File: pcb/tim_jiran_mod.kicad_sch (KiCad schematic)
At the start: 110 parts, among them J3 MJ-4PP-9, J6 MJ-4PP-9, SW1 SW_PUSH, SW10 SW_PUSH, SW11 SW_PUSH, SW12 SW_PUSH, SW13 SW_PUSH, SW14 SW_PUSH, SW15 SW_PUSH, SW16 SW_PUSH, SW17 SW_PUSH, SW18 SW_PUSH, SW19 SW_RESET, SW2 SW_PUSH, SW20 SW_PUSH, SW21 SW_PUSH, SW22 SW_PUSH, SW23 SW_PUSH, SW24 SW_PUSH, SW25 SW_PUSH, SW26 SW_PUSH, SW27 SW_PUSH, SW28 SW_PUSH, SW29 SW_PUSH, SW3 SW_PUSH, SW30 SW_PUSH, SW31 SW_PUSH, SW32 SW_PUSH, SW33 SW_PUSH, SW34 SW_PUSH, SW35 SW_PUSH, SW36 SW_PUSH, SW37 SW_PUSH, SW38 SW_PUSH, SW39 SW_PUSH, SW4 SW_PUSH, SW40 SW_PUSH, SW41 SW_PUSH, SW42 SW_RESET, SW43 SW_PUSH, SW44 SW_PUSH, SW45 SW_PUSH, SW46 SW_PUSH, SW5 SW_PUSH, SW6 SW_PUSH, SW7 SW_PUSH, SW8 SW_PUSH, SW9 SW_PUSH, U1 Raspberry_Pie_Pico, U2 Raspberry_Pie_Pico

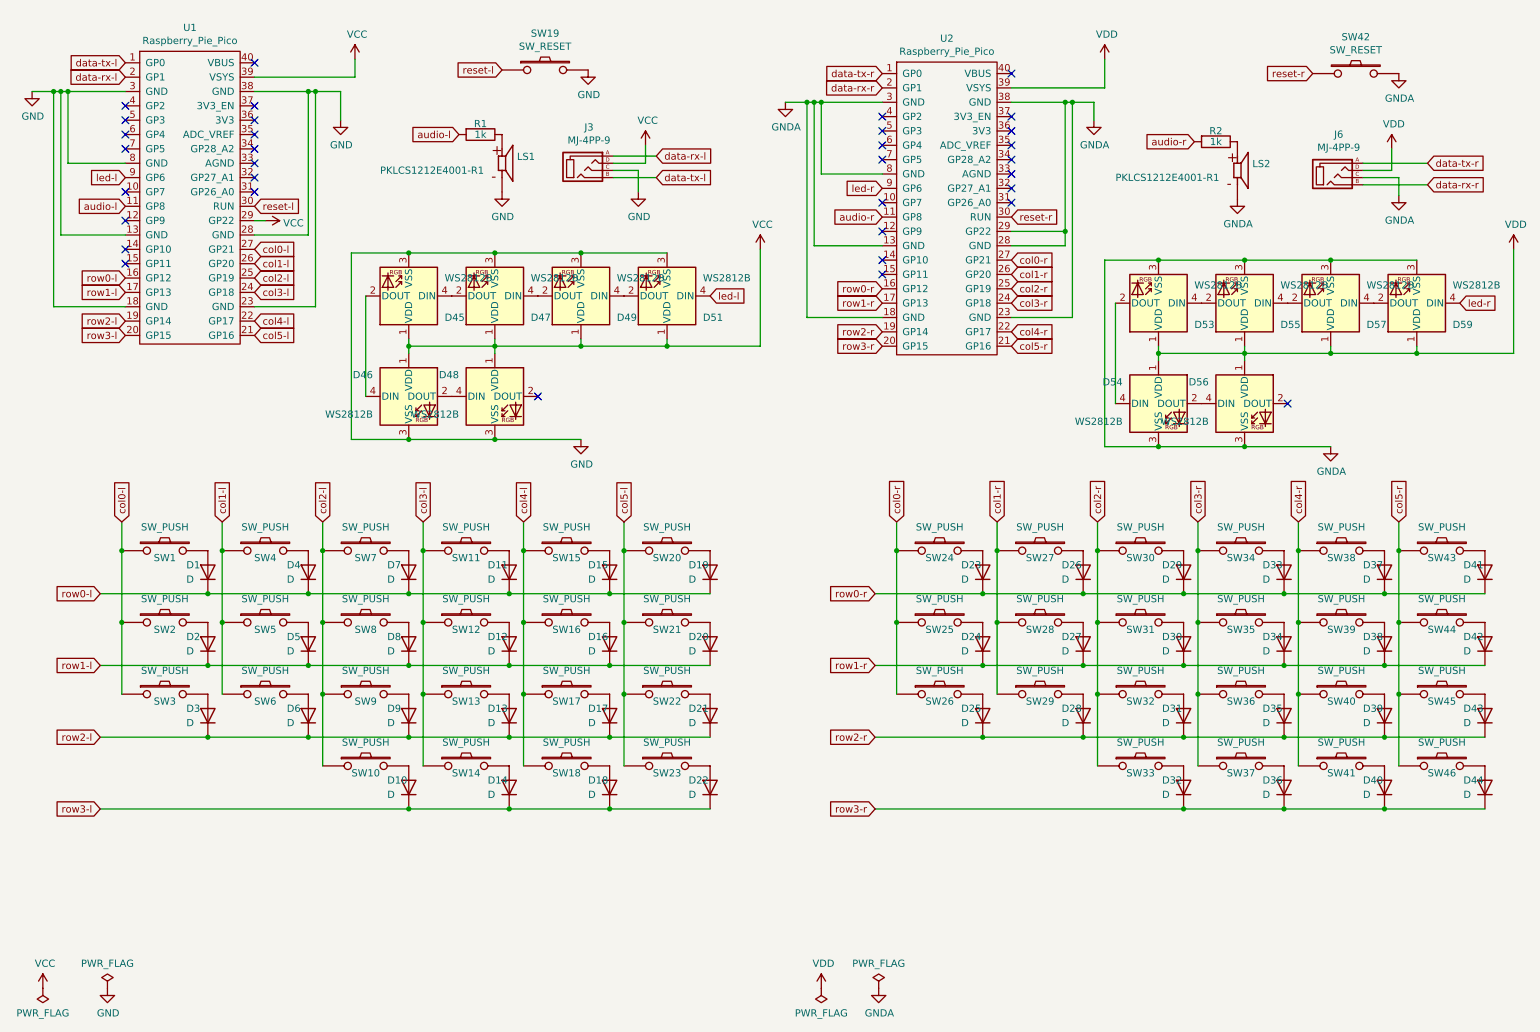
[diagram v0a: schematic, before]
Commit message: добавил дополнительный ряд клавиш в раскладку (в схему и в исходник)
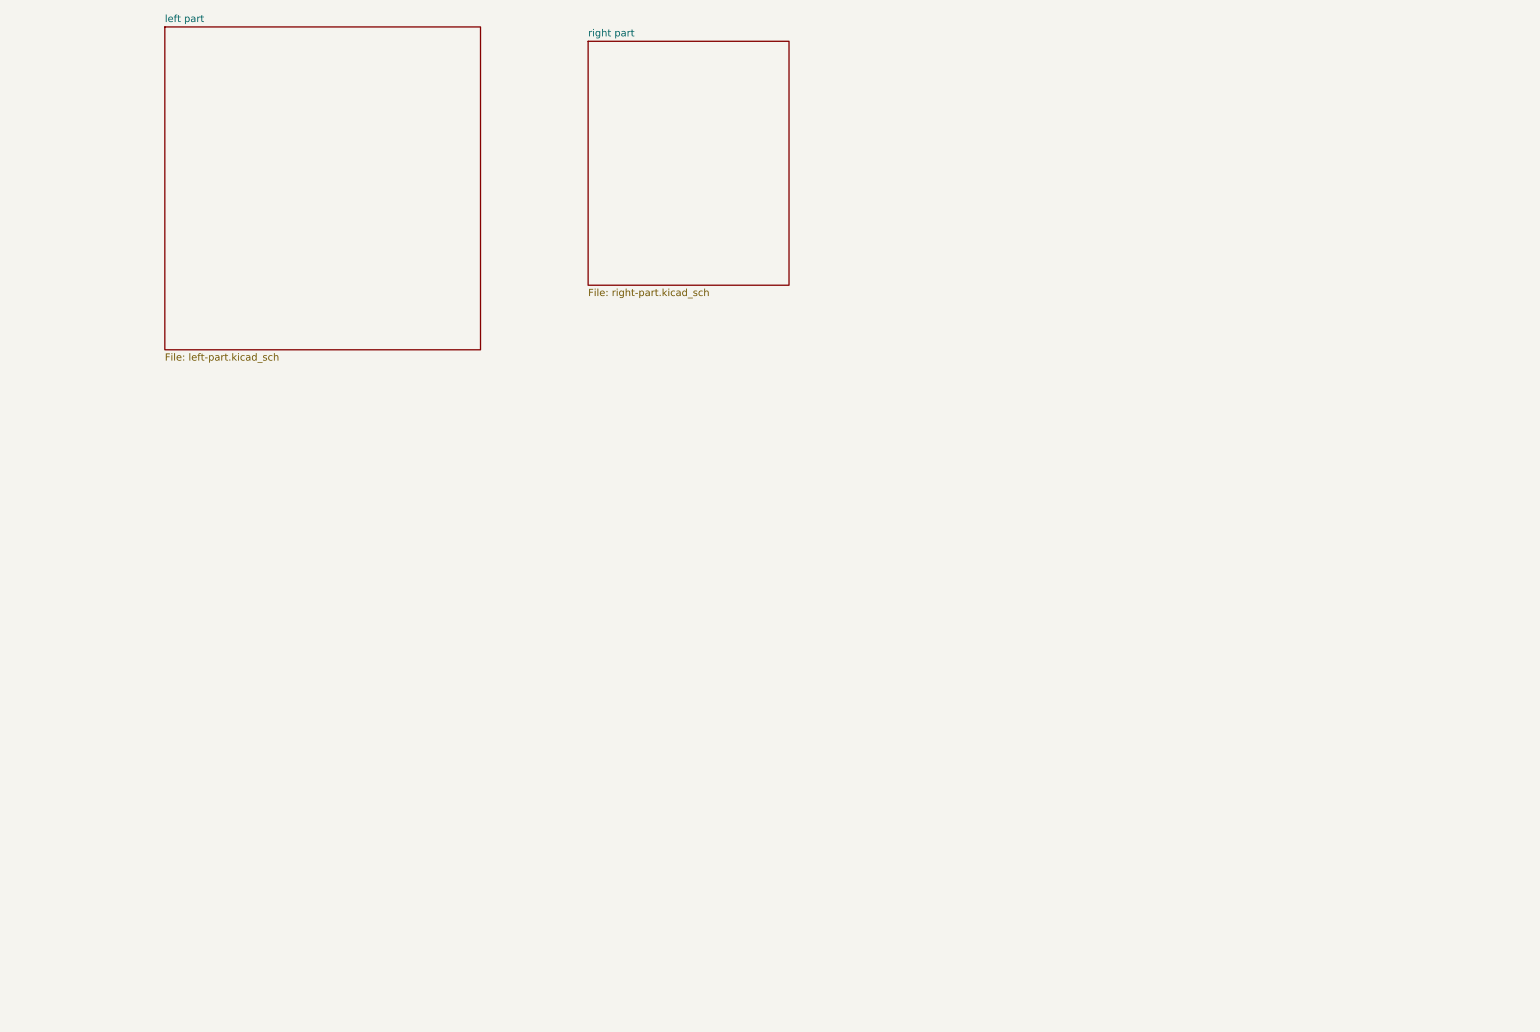
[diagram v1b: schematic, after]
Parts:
- removed D1, D10, D11, D12, D13, D14, D15, D16, D17, D18, D19, D2, D20, D21, D22, D23, D24, D25, D26, D27, D28, D29, D3, D30, D31, D32, D33, D34, D35, D36, D37, D38, D39, D4, D40, D41, D42, D43, D44, D5, D6, D7, D8, D9: D, Keebio-Parts:Diode-Hybrid-Back, symbol Device:D
- removed D45, D46, D47, D48, D49, D51, D53, D54, D55, D56, D57, D59: WS2812B, Yoichiro:LED_WS2812B, symbol LED:WS2812B
- removed J3, J6: MJ-4PP-9, kbd:MJ-4PP-9_1side, symbol kbd:MJ-4PP-9
- removed LS1, LS2: PKLCS1212E4001-R1, Yoichiro:SPKR_PKLCS1212E4001-R1, symbol PKLCS1212E4001-R1:PKLCS1212E4001-R1
- removed R1, R2: 1k, Keebio-Parts:Resistor-Hybrid-Back, symbol Device:R
- removed SW1, SW10, SW11, SW12, SW13, SW14, SW15, SW16, SW17, SW18, SW2, SW20, SW21, SW22, SW23, SW24, SW25, SW26, SW27, SW28, SW29, SW3, SW30, SW31, SW32, SW33, SW34, SW35, SW36, SW37, SW38, SW39, SW4, SW40, SW41, SW43, SW44, SW45, SW46, SW5, SW6, SW7, SW8, SW9: SW_PUSH, Yoichiro:CherryMX_Choco_Hotswap, symbol kbd:SW_PUSH
- removed SW19, SW42: SW_RESET, kbd:ResetSW_1side, symbol kbd:SW_PUSH
- removed U1, U2: Raspberry_Pie_Pico, Yoichiro:Raspberry_Pi_Pico, symbol yoichiro:Raspberry_Pie_Pico
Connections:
- no-connect marks 34 -> 0
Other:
- added sheet left part (left-part.kicad_sch)
- added sheet right part (right-part.kicad_sch)
